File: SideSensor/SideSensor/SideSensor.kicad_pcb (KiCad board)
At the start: 2 copper layers, 35 x 7.1 mm, 6 parts, among them J1 SH_03, U1 S7136

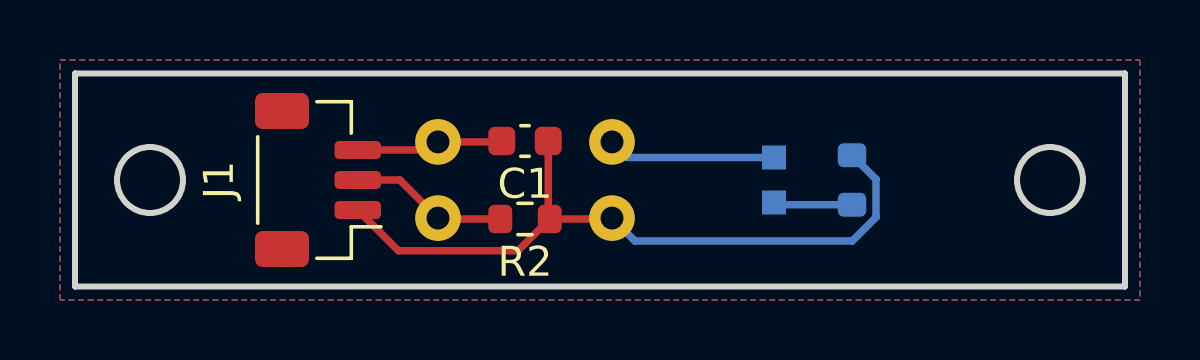
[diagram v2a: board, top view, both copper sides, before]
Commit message: add logo
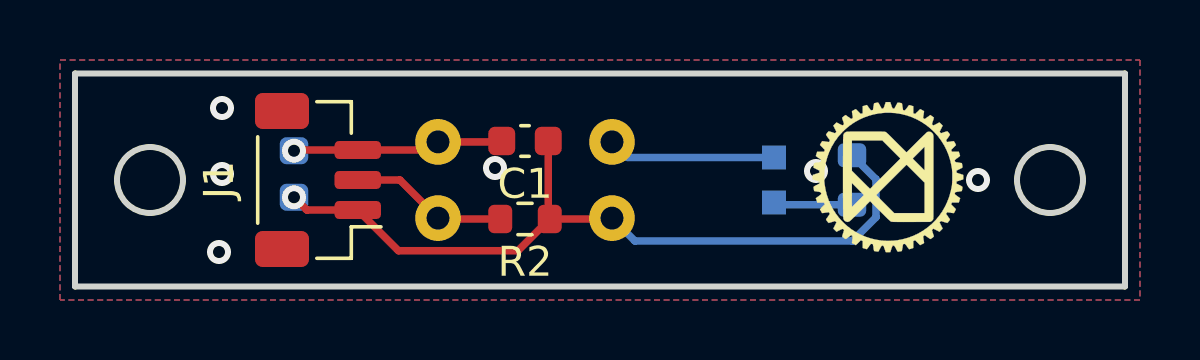
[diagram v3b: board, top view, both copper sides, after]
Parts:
- added C2: 1u, Capacitor_SMD:C_0603_1608Metric, B.Cu at (151.8, 108.8)
- added G***: LOGO, Symbol:SH-Logo_5x5mm, F.Cu at (171.6, 108.9)
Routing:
- net +5V: track 23.9 -> 26.3 mm, vias 0 -> 1
- net GND: track 4.92 -> 7.06 mm, vias 0 -> 7
